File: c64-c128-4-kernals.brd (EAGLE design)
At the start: 21.9 x 40.6 mm, 15 parts, among them IC1 27C512, IC2 PIC12F629P

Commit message: using larger pads
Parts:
- IC1: value 27C512 -> 27C256/512; device ic-package:DIL28-6 -> c64switchless:IC-PACKAGE_EDIT_DIL28SPECIAL
- IC2: value PIC12F629P -> MICROCHIP_PIC12F629P; device microchip:DIL8 -> c64switchless:MICROCHIP_DIL8
- R1, R2, R3: device resistor:0207/10 -> c64switchless:RCL_0207/10
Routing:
- net VCC: track 11.4 -> 9.94 mm
- net A14: track 29.8 -> 30.9 mm
- net N$16: track 18.7 -> 19.7 mm
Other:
- board text added: "Rev 1.1 by discoHR 2016"
- board text removed: "Rev 1.0 by discoHR 2016"
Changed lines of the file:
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@@
 <wire x1="21.895" y1="40.63" x2="0" y2="40.63" width="0" layer="20"/>
 <wire x1="0" y1="40.63" x2="0" y2="0" width="0" layer="20"/>
-<text x="10.795" y="36.195" size="0.4572" layer="25" font="vector" align="bottom-center">Rev 1.0 by discoHR 2016</text>
-<text x="10.795" y="34.925" size="0.381" layer="25" font="vector" align="bottom-center">based on Bwack's 27C256 24-pin</text>
-<text x="10.795" y="37.465" size="0.4572" layer="25" font="vector" align="bottom-center">28-pin multi-kernal adapter</text>
-<text x="10.795" y="34.29" size="0.381" layer="25" font="vector" align="bottom-center">multi-kernal adapter</text>
+<text x="10.795" y="36.195" size="0.4572" layer="25" font="vector" align="bottom-center">Rev 1.1 by discoHR 2016</text>
+<text x="11.43" y="34.925" size="0.381" layer="25" font="vector" align="bottom-center">based on Bwack's 27C256 24-pin</text>
+<text x="11.43" y="37.465" size="0.4572" layer="25" font="vector" align="bottom-center">28-pin multi-kernal adapter</text>
+<text x="11.43" y="34.29" size="0.381" layer="25" font="vector" align="bottom-center">multi-kernal adapter</text>
 <text x="8.255" y="38.735" size="0.6096" layer="25" font="vector" align="bottom-center">C64/C128</text>
 <text x="9.525" y="19.685" size="0.254" layer="25" font="vector">OPEN: 4 kernals (27C512)</text>
 <text x="9.525" y="19.05" size="0.254" layer="25" font="vector">CLOSED: 2 kernals (27C256)</text>
-<text x="15.24" y="36.195" size="0.6096" layer="26" rot="MR0" align="center-left">NC</text>
+<text x="15.24" y="36.195" size="0.6096" layer="26" font="vector" rot="MR0" align="center-left">NC</text>
 <text x="9.525" y="28.1178" size="1.016" layer="25" ratio="10">IC2</text>
 </plain>
@@
 </element>
 <element name="GREEN" library="wirepad" package="2,15/1,0" value="" x="9.525" y="2.54" smashed="yes">
-<attribute name="NAME" x="10.033" y="1.016" size="0.4064" layer="25" font="vector" ratio="10" align="top-center"/>
+<attribute name="NAME" x="9.398" y="1.016" size="0.4064" layer="25" font="vector" ratio="10" align="top-center"/>
 <attribute name="VALUE" x="9.525" y="3.14" size="0.0254" layer="27"/>
 </element>
@@
 <attribute name="VALUE" x="6.985" y="3.14" size="0.0254" layer="27"/>
 </element>
-<element name="IC1" library="ic-package" package="DIL28-6" value="27C512" x="12.065" y="22.225" smashed="yes" rot="R270">
+<element name="IC1" library="c64switchless" package="IC-PACKAGE_EDIT_DIL28SPECIAL" value="27C256/512" x="12.065" y="22.225" smashed="yes" rot="R270">
 <attribute name="NAME" x="11.43" y="21.59" size="1.016" layer="25" font="vector" ratio="10" align="bottom-center"/>
 </element>
-<element name="IC2" library="microchip" package="DIL8" value="PIC12F629P" x="10.795" y="28.575" smashed="yes" rot="R270">
+<element name="IC2" library="c64switchless" package="MICROCHIP_DIL8" value="MICROCHIP_PIC12F629P" x="10.795" y="28.575" smashed="yes" rot="R270">
 <attribute name="OC_FARNELL" value="1292253" x="10.795" y="28.575" size="1.778" layer="27" rot="R270" display="off"/>
 <attribute name="MPN" value="PIC12F629-I/P" x="10.795" y="28.575" size="1.778" layer="27" rot="R270" display="off"/>
@@
 <attribute name="VALUE" x="13.97" y="4.445" size="1.27" layer="28" rot="MR90"/>
 </element>
-<element name="R1" library="resistor" package="0207/10" value="2.2k" x="8.255" y="11.43" smashed="yes" rot="R90">
+<element name="R1" library="c64switchless" package="RCL_0207/10" value="2.2k" x="8.255" y="11.43" smashed="yes" rot="R90">
 <attribute name="NAME" x="8.001" y="12.192" size="0.8128" layer="25" font="vector" ratio="10" rot="R90" align="top-right"/>
 </element>
-<element name="R2" library="resistor" package="0207/10" value="2.2k" x="10.795" y="11.43" smashed="yes" rot="R90">
+<element name="R2" library="c64switchless" package="RCL_0207/10" value="2.2k" x="10.795" y="11.43" smashed="yes" rot="R90">
 <attribute name="NAME" x="10.541" y="12.192" size="0.8128" layer="25" font="vector" ratio="10" rot="R90" align="top-right"/>
 </element>
-<element name="R3" library="resistor" package="0207/10" value="2.2k" x="13.335" y="11.43" smashed="yes" rot="R90">
+<element name="R3" library="c64switchless" package="RCL_0207/10" value="2.2k" x="13.335" y="11.43" smashed="yes" rot="R90">
 <attribute name="NAME" x="13.081" y="12.192" size="0.8128" layer="25" font="vector" ratio="10" rot="R90" align="top-right"/>
 </element>
@@
 <vertex x="0.635" y="40.005"/>
 </polygon>
-<wire x1="1.905" y1="38.735" x2="3.175" y2="38.735" width="0.6096" layer="16"/>
-<wire x1="3.175" y1="38.735" x2="3.175" y2="37.465" width="0.6096" layer="16"/>
-<wire x1="3.175" y1="37.465" x2="6.985" y2="37.465" width="0.6096" layer="16"/>
-<wire x1="6.985" y1="37.465" x2="6.985" y2="32.385" width="0.6096" layer="16"/>
+<wire x1="1.905" y1="38.735" x2="3.175" y2="37.465" width="0.508" layer="16"/>
+<wire x1="3.175" y1="37.465" x2="5.715" y2="37.465" width="0.508" layer="16"/>
+<wire x1="5.715" y1="37.465" x2="6.985" y2="36.195" width="0.508" layer="16"/>
+<wire x1="6.985" y1="36.195" x2="6.985" y2="32.385" width="0.508" layer="16"/>
+<wire x1="14.605" y1="2.54" x2="6.985" y2="32.385" width="0" layer="19" extent="1-1"/>
 </signal>
 <signal name="GND" class="1">
@@
 <contactref element="R3" pad="2"/>
 <contactref element="IC2" pad="3"/>
-<wire x1="7.06755" y1="26.1366" x2="7.06755" y2="27.2034" width="0.4064" layer="16"/>
-<wire x1="13.335" y1="19.86915" x2="7.06755" y2="26.1366" width="0.4064" layer="16"/>
-<wire x1="13.335" y1="16.51" x2="13.335" y2="19.86915" width="0.4064" layer="16"/>
-<wire x1="7.06755" y1="27.2034" x2="6.985" y2="27.305" width="0.4064" layer="16"/>
 <wire x1="19.685" y1="36.195" x2="18.415" y2="34.925" width="0.4064" layer="1"/>
-<wire x1="18.415" y1="34.925" x2="14.605" y2="34.925" width="0.4064" layer="1"/>
-<wire x1="14.605" y1="34.925" x2="6.985" y2="27.305" width="0.4064" layer="1"/>
+<wire x1="18.415" y1="34.925" x2="12.7" y2="34.925" width="0.4064" layer="1"/>
+<wire x1="6.985" y1="27.305" x2="13.335" y2="20.955" width="0.4064" layer="16"/>
+<wire x1="13.335" y1="20.955" x2="13.335" y2="16.51" width="0.4064" layer="16"/>
+<wire x1="12.7" y1="34.925" x2="8.255" y2="30.48" width="0.4064" layer="1"/>
+<wire x1="8.255" y1="30.48" x2="8.255" y2="28.575" width="0.4064" layer="1"/>
+<wire x1="8.255" y1="28.575" x2="6.985" y2="27.305" width="0.4064" layer="1"/>
 </signal>
 <signal name="N$3">
@@
 <contactref element="R1" pad="1"/>
 <contactref element="RED" pad="1"/>
-<wire x1="1.905" y1="2.54" x2="3.81" y2="4.445" width="0.6096" layer="16"/>
-<wire x1="3.81" y1="4.445" x2="6.35" y2="4.445" width="0.6096" layer="16"/>
-<wire x1="6.35" y1="4.445" x2="8.255" y2="6.35" width="0.6096" layer="16"/>
+<wire x1="1.905" y1="2.54" x2="3.81" y2="4.445" width="0.4064" layer="16"/>
+<wire x1="3.81" y1="4.445" x2="6.35" y2="4.445" width="0.4064" layer="16"/>
+<wire x1="6.35" y1="4.445" x2="8.255" y2="6.35" width="0.4064" layer="16"/>
 </signal>
 <signal name="N$29">
 <contactref element="BLUE" pad="1"/>
 <contactref element="R2" pad="1"/>
-<wire x1="6.985" y1="2.54" x2="10.795" y2="6.35" width="0.6096" layer="16"/>
+<wire x1="6.985" y1="2.54" x2="10.795" y2="6.35" width="0.4064" layer="16"/>
 </signal>
 <signal name="N$30">
 <contactref element="R3" pad="1"/>
 <contactref element="GREEN" pad="1"/>
-<wire x1="9.525" y1="2.54" x2="13.335" y2="6.35" width="0.6096" layer="16"/>
+<wire x1="9.525" y1="2.54" x2="13.335" y2="6.35" width="0.4064" layer="16"/>
 </signal>
 <signal name="N$31">
@@
 <contactref element="IC2" pad="6"/>
 <contactref element="SJ1" pad="2"/>
-<wire x1="8.40105" y1="25.0698" x2="8.40105" y2="19.7358" width="0.4064" layer="1"/>
-<wire x1="14.26845" y1="30.9372" x2="8.40105" y2="25.0698" width="0.4064" layer="1"/>
-<wire x1="14.9352" y1="30.9372" x2="14.26845" y2="30.9372" width="0.4064" layer="1"/>
-<wire x1="15.60195" y1="30.27045" x2="14.9352" y2="30.9372" width="0.4064" layer="1"/>
-<wire x1="15.60195" y1="28.2702" x2="15.60195" y2="30.27045" width="0.4064" layer="1"/>
-<wire x1="14.6685" y1="27.33675" x2="15.60195" y2="28.2702" width="0.4064" layer="1"/>
-<wire x1="8.40105" y1="19.7358" x2="8.382" y2="19.685" width="0.4064" layer="1"/>
-<wire x1="14.6685" y1="27.33675" x2="14.605" y2="27.305" width="0.4064" layer="1"/>
+<wire x1="14.605" y1="27.305" x2="15.875" y2="28.575" width="0.4064" layer="1"/>
+<wire x1="15.875" y1="28.575" x2="15.875" y2="30.48" width="0.4064" layer="1"/>
+<wire x1="15.875" y1="30.48" x2="15.24" y2="31.115" width="0.4064" layer="1"/>
+<wire x1="15.24" y1="31.115" x2="13.97" y2="31.115" width="0.4064" layer="1"/>
+<wire x1="13.97" y1="31.115" x2="9.525" y2="26.67" width="0.4064" layer="1"/>
+<wire x1="9.525" y1="26.67" x2="9.525" y2="23.495" width="0.4064" layer="1"/>
+<wire x1="9.525" y1="23.495" x2="8.255" y2="22.225" width="0.4064" layer="1"/>
+<wire x1="8.255" y1="22.225" x2="8.255" y2="19.812" width="0.4064" layer="1"/>
+<wire x1="8.255" y1="19.812" x2="8.382" y2="19.685" width="0.4064" layer="1"/>
 </signal>
 </signals>
+<errors>
+</errors>
 </board>
 </drawing>

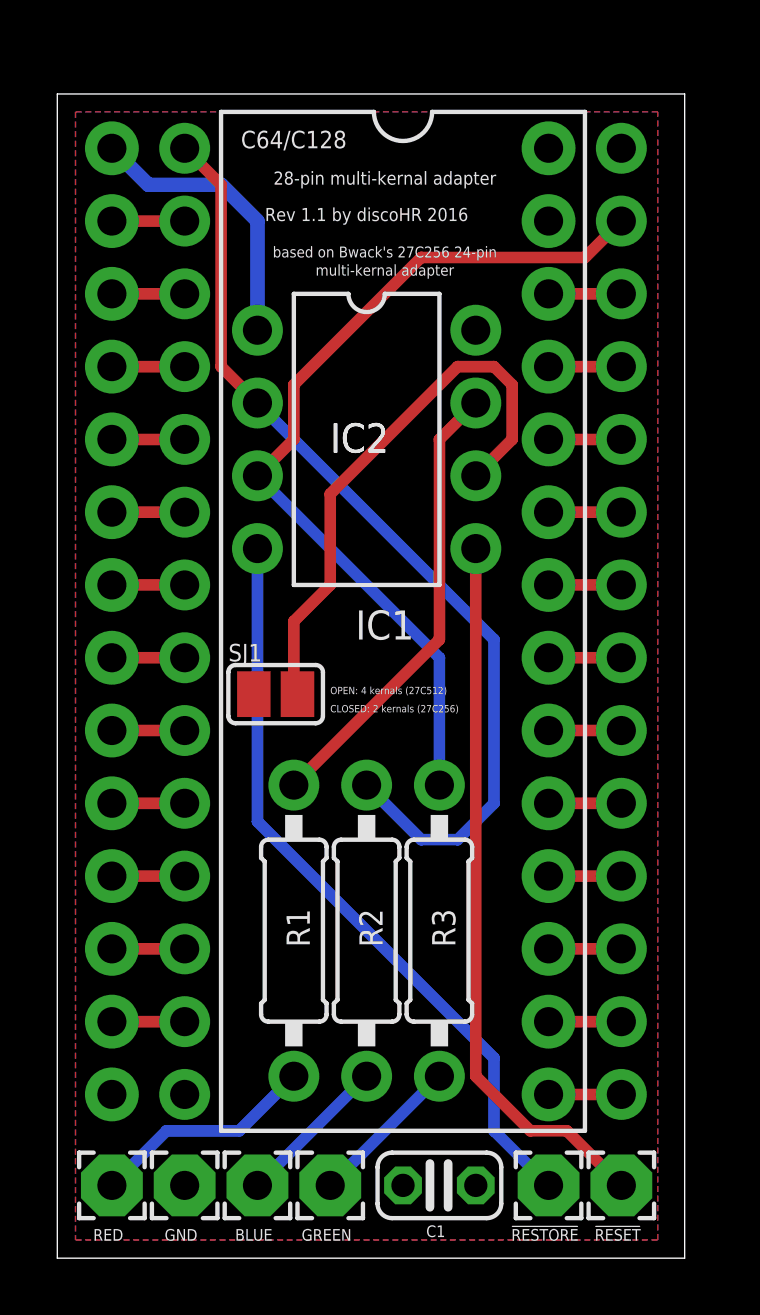
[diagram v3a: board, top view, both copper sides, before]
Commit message: bumped resistor values significantly because the LED is still too bright at 6.7k increased the board size a bit and rerouted most of the traces
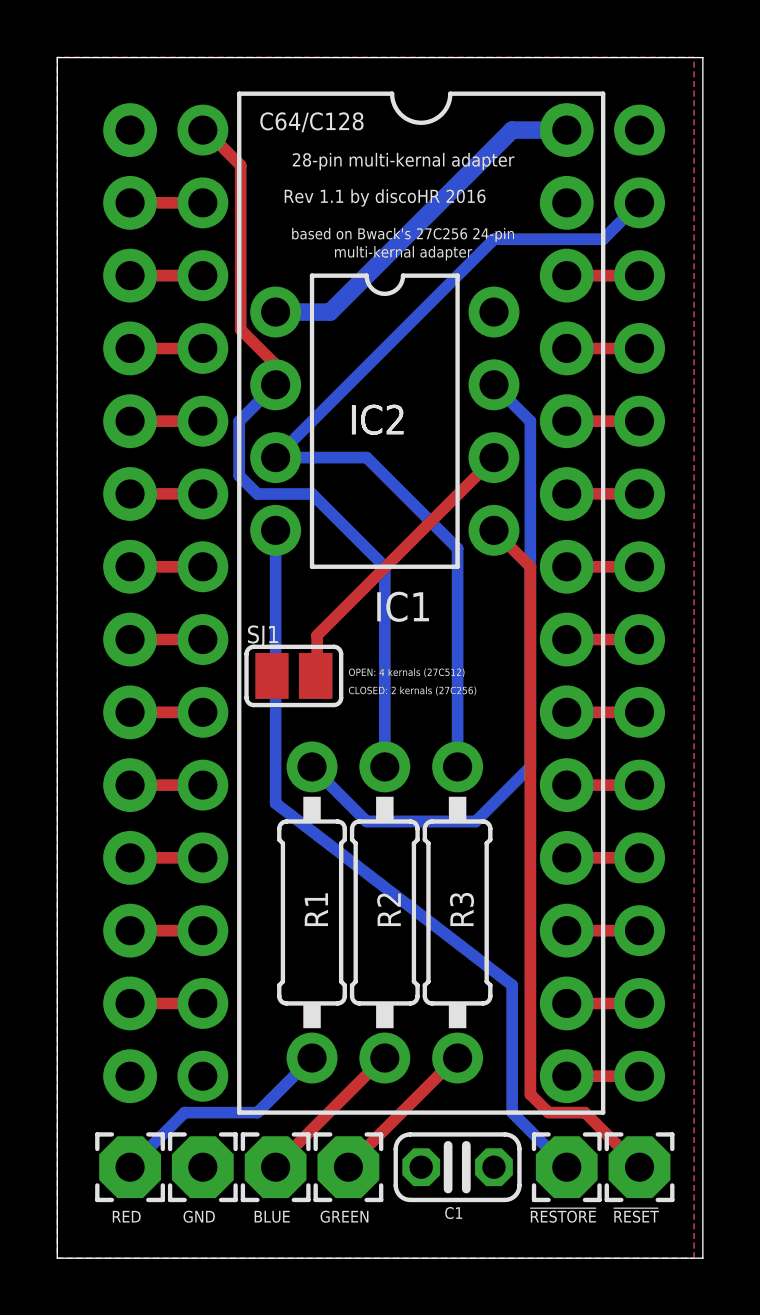
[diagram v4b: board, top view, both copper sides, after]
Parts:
- R1: value 2.2k -> 6.7k
- R2: value 2.2k -> 10k
- R3: value 2.2k -> 12k
- moved SJ1 0.90 mm to (8.26, 20.3)
- moved !RESET! 0.90 mm to (20.3, 3.17)
- moved !RESTORE! 0.90 mm to (17.8, 3.17)
- moved IC2 0.90 mm to (11.4, 29.2)
- moved J2 0.90 mm to (17.8, 6.35)
- moved J1 0.90 mm to (2.54, 6.35)
- moved RED 0.90 mm to (2.54, 3.17)
- moved BLUE 0.90 mm to (7.62, 3.17)
- moved C1 0.90 mm to (14.0, 3.17)
- moved GND 0.90 mm to (5.08, 3.17)
- moved GREEN 0.90 mm to (10.2, 3.17)
- moved R1 0.90 mm to (8.89, 12.1)
- moved R2 0.90 mm to (11.4, 12.1)
- moved R3 0.90 mm to (14.0, 12.1)
- moved IC1 0.90 mm to (12.7, 22.9)
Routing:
- net N$16: track 19.7 -> 10.2 mm
- net N$1: track 16.0 -> 23.1 mm
- net A15: track 33.1 -> 27.1 mm
- net VCC: track 9.94 -> 12.8 mm
- net A14: track 30.9 -> 31.7 mm
- net N$31: track 26.4 -> 27.1 mm
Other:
- board size 21.9 x 40.6 mm -> 22.5 x 41.9 mm

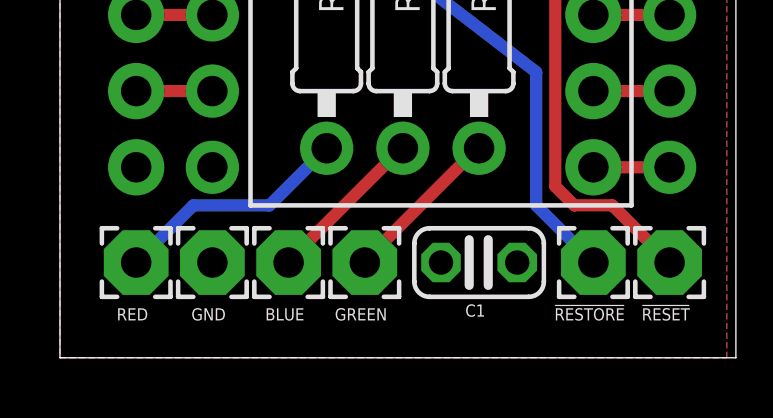
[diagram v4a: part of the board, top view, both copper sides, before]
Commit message: using 6.7k value for R1, R2 and R3
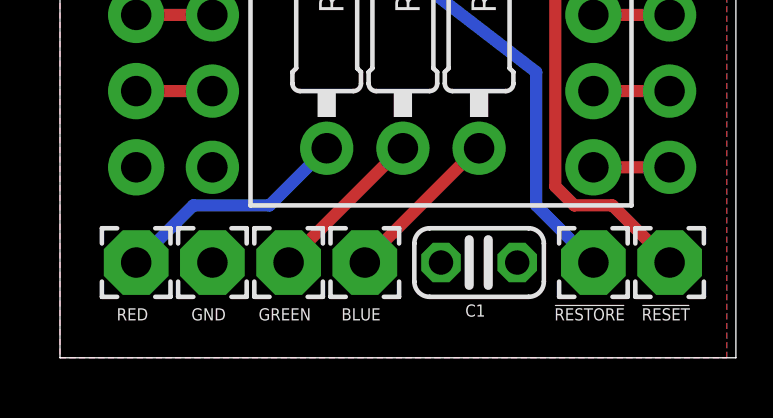
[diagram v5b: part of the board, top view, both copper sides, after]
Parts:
- R2: value 10k -> 6.7k
- R3: value 12k -> 6.7k
- moved BLUE 2.54 mm to (10.2, 3.17)
- moved GREEN 2.54 mm to (7.62, 3.17)
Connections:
- net N$29: now also GREEN.1; no longer BLUE.1
- net N$30: now also BLUE.1; no longer GREEN.1
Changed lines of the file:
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@@
 <text x="15.875" y="36.83" size="0.6096" layer="26" font="vector" rot="MR0" align="center-left">NC</text>
 <text x="10.16" y="28.7528" size="1.016" layer="25" ratio="10">IC2</text>
-<dimension x1="0" y1="0" x2="22.53" y2="0" x3="11.265" y3="-3.175" textsize="1.778" layer="20"/>
-<dimension x1="22.53" y1="0" x2="22.53" y2="41.9" x3="25.4" y3="20.95" textsize="1.778" layer="20"/>
 </plain>
 <attributes>
@@
 <attribute name="VALUE" x="17.78" y="3.775" size="0.0254" layer="27"/>
 </element>
-<element name="GREEN" library="wirepad" package="2,15/1,0" value="" x="10.16" y="3.175" smashed="yes">
+<element name="BLUE" library="wirepad" package="2,15/1,0" value="" x="10.16" y="3.175" smashed="yes">
 <attribute name="NAME" x="10.033" y="1.651" size="0.4064" layer="25" font="vector" ratio="10" align="top-center"/>
 <attribute name="VALUE" x="10.16" y="3.775" size="0.0254" layer="27"/>
@@
 <attribute name="VALUE" x="5.08" y="3.775" size="0.0254" layer="27"/>
 </element>
-<element name="BLUE" library="wirepad" package="2,15/1,0" value="" x="7.62" y="3.175" smashed="yes">
+<element name="GREEN" library="wirepad" package="2,15/1,0" value="" x="7.62" y="3.175" smashed="yes">
 <attribute name="NAME" x="7.493" y="1.651" size="0.4064" layer="25" font="vector" ratio="10" align="top-center"/>
 <attribute name="VALUE" x="7.62" y="3.775" size="0.0254" layer="27"/>
@@
 <attribute name="NAME" x="8.636" y="12.827" size="0.8128" layer="25" font="vector" ratio="10" rot="R90" align="top-right"/>
 </element>
-<element name="R2" library="c64switchless" package="RCL_0207/10" value="10k" x="11.43" y="12.065" smashed="yes" rot="R90">
+<element name="R2" library="c64switchless" package="RCL_0207/10" value="6.7k" x="11.43" y="12.065" smashed="yes" rot="R90">
 <attribute name="NAME" x="11.176" y="12.827" size="0.8128" layer="25" font="vector" ratio="10" rot="R90" align="top-right"/>
 </element>
-<element name="R3" library="c64switchless" package="RCL_0207/10" value="12k" x="13.97" y="12.065" smashed="yes" rot="R90">
+<element name="R3" library="c64switchless" package="RCL_0207/10" value="6.7k" x="13.97" y="12.065" smashed="yes" rot="R90">
 <attribute name="NAME" x="13.716" y="12.827" size="0.8128" layer="25" font="vector" ratio="10" rot="R90" align="top-right"/>
 </element>
@@
 </signal>
 <signal name="N$29">
-<contactref element="BLUE" pad="1"/>
+<contactref element="GREEN" pad="1"/>
 <contactref element="R2" pad="1"/>
 <wire x1="7.60095" y1="3.2004" x2="11.33475" y2="6.9342" width="0.4064" layer="1"/>
@@
 <signal name="N$30">
 <contactref element="R3" pad="1"/>
-<contactref element="GREEN" pad="1"/>
+<contactref element="BLUE" pad="1"/>
 <wire x1="10.1346" y1="3.2004" x2="13.8684" y2="6.9342" width="0.4064" layer="1"/>
 <wire x1="13.8684" y1="6.9342" x2="13.97" y2="6.985" width="0.4064" layer="1"/>
